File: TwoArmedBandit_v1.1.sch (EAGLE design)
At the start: 36 parts, among them J1 Nose_L, J10 LED_L, J11 Nose_R, J12 Lick_R, J13 Aux, J14 POWER_JACK, J15 Valve_R, J16 DAQ_L, J17 LED_R, J18 V_valve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

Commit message: Fix wiring of V_valve; Update version to v1.1
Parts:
- FRAME1: DESIGNER (none) -> Ofer Mazor; VERSION (none) -> v01.1
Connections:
- removed net VCC: J18.1, JP1.2, U1.10
- new net V_VALVE: J15.1, J18.1, J5.1, J7.1, JP1.2, U1.10
- net VIN: no longer J15.1, J5.1, J7.1
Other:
- note added: "1.1"
- note added: "Ofer Mazor"
- moved on the sheet: J16, J19, J8, J9

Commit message: Swap pins for Aux-1/Aux-2
In order for Aux-1-Laser to have PWM, needed to change
Aux-1 to D11 and Aux-2 to D12.
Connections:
- net AUX_1_LASER: now also B1.*D11; no longer B1.D12
- net AUX_2: now also B1.D12; no longer B1.*D11
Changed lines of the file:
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@@
 <drawing>
 <settings>
-<setting alwaysvectorfont="no"/>
+<setting alwaysvectorfont="yes"/>
 <setting verticaltext="up"/>
 </settings>
@@
 </segment>
 <segment>
+<pinref part="J23" gate="G$1" pin="OUT"/>
+<wire x1="228.6" y1="124.46" x2="233.68" y2="124.46" width="0.1524" layer="91"/>
+<label x="233.68" y="124.46" size="1.27" layer="95" xref="yes"/>
+</segment>
+<segment>
+<pinref part="B1" gate="G$1" pin="*D11"/>
+<wire x1="43.18" y1="137.16" x2="45.72" y2="137.16" width="0.1524" layer="91"/>
+<label x="45.72" y="137.16" size="1.27" layer="95" xref="yes"/>
+</segment>
+</net>
+<net name="AUX_2" class="0">
+<segment>
+<pinref part="J19" gate="G$1" pin="2"/>
+<wire x1="226.06" y1="63.5" x2="223.52" y2="63.5" width="0.1524" layer="91"/>
+<label x="223.52" y="63.5" size="1.27" layer="95" rot="R180" xref="yes"/>
+</segment>
+<segment>
+<pinref part="J13" gate="G$1" pin="4"/>
+<wire x1="226.06" y1="152.4" x2="223.52" y2="152.4" width="0.1524" layer="91"/>
+<label x="223.52" y="152.4" size="1.27" layer="95" rot="R180" xref="yes"/>
+</segment>
+<segment>
 <pinref part="B1" gate="G$1" pin="D12"/>
 <wire x1="43.18" y1="134.62" x2="45.72" y2="134.62" width="0.1524" layer="91"/>
 <label x="45.72" y="134.62" size="1.27" layer="95" xref="yes"/>
 </segment>
-<segment>
-<pinref part="J23" gate="G$1" pin="OUT"/>
-<wire x1="228.6" y1="124.46" x2="233.68" y2="124.46" width="0.1524" layer="91"/>
-<label x="233.68" y="124.46" size="1.27" layer="95" xref="yes"/>
-</segment>
-</net>
-<net name="AUX_2" class="0">
-<segment>
-<pinref part="J19" gate="G$1" pin="2"/>
-<wire x1="226.06" y1="63.5" x2="223.52" y2="63.5" width="0.1524" layer="91"/>
-<label x="223.52" y="63.5" size="1.27" layer="95" rot="R180" xref="yes"/>
-</segment>
-<segment>
-<pinref part="J13" gate="G$1" pin="4"/>
-<wire x1="226.06" y1="152.4" x2="223.52" y2="152.4" width="0.1524" layer="91"/>
-<label x="223.52" y="152.4" size="1.27" layer="95" rot="R180" xref="yes"/>
-</segment>
-<segment>
-<pinref part="B1" gate="G$1" pin="*D11"/>
-<wire x1="43.18" y1="137.16" x2="45.72" y2="137.16" width="0.1524" layer="91"/>
-<label x="45.72" y="137.16" size="1.27" layer="95" xref="yes"/>
-</segment>
-</net>
+</net>

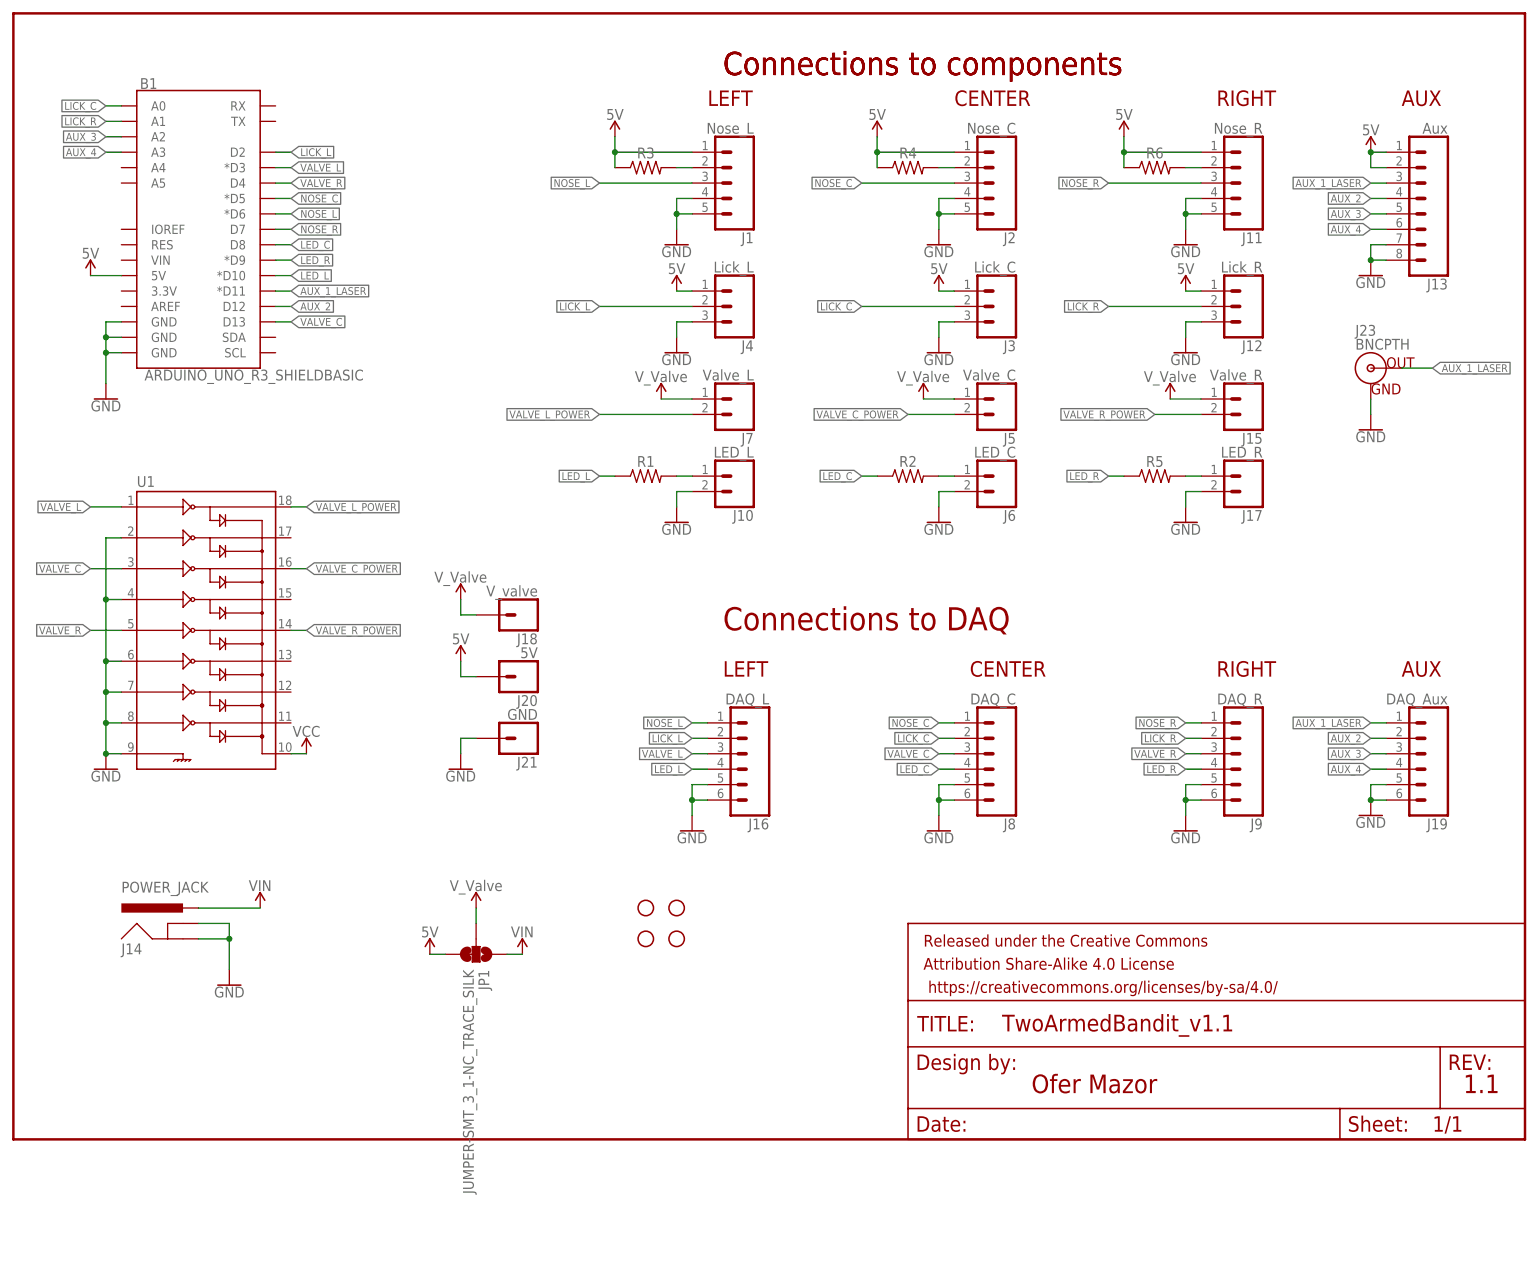
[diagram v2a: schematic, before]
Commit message: Add optional RC filter to lick sensor output
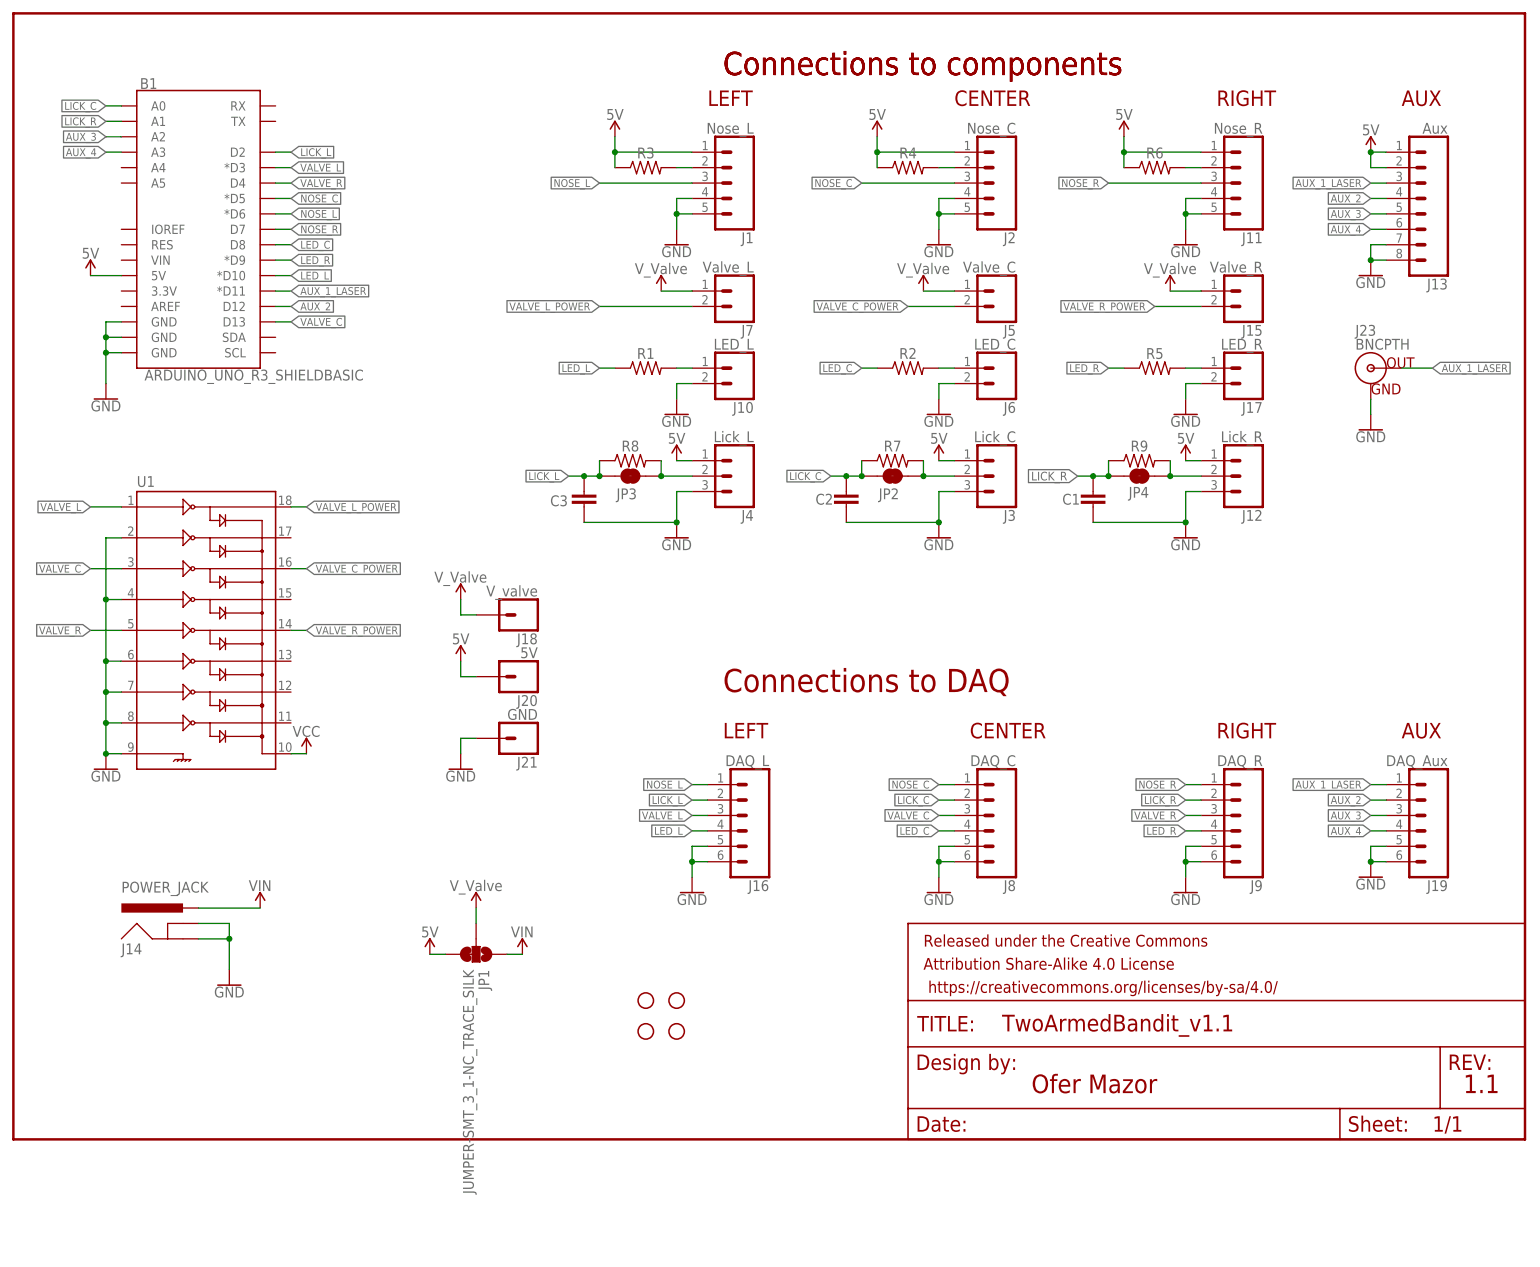
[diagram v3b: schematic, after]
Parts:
- added C1, C2, C3: (no value), capacitor-wima:C5/2.5
- added JP2, JP3, JP4: JUMPER-SMT_2_NC_TRACE_NO-SILK, SparkFun-Jumpers:JUMPER-SMT_2_NC_TRACE_NO-SILK
- added R7, R8, R9: 160, rcl:R-US_0309/12
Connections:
- new net N$6: J12.2, JP4.2, R9.2
- new net N$7: J3.2, JP2.2, R7.2
- new net N$8: J4.2, JP3.2, R8.2
- net GND: now also C1.2, C2.2, C3.2
- net LICK_C: now also C2.1, JP2.1, R7.1; no longer J3.2
- net LICK_L: now also C3.1, JP3.1, R8.1; no longer J4.2
- net LICK_R: now also C1.1, JP4.1, R9.1; no longer J12.2
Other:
- moved on the sheet: J10, J12, J15, J16, J17, J19, J3, J4, J5, J6, J7, J8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
